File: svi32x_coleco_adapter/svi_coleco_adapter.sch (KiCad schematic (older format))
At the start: 62 parts, among them J1 Conn_01x09, J2 Conn_01x09, J3 COLECO cartridge slot, J4 SVI external bus connector, T1 NPN_BCE_9014B, T2 NPN_BCE_9014B, U1 74LS244, U10 27C64, U11 L79L05, U2 74LS244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

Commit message: Add files via upload
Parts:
- added C30, C31, C32, C33, C34, C35, C36, C37: 100nf, Capacitor_THT:C_Disc_D7.0mm_W2.5mm_P5.00mm, symbol agg-kicad:C
- C1, C12, C14, C15, C16, C19, C2, C21, C3, C4, C5, C6, C7, C8, C9: footprint Capacitor_THT:C_Disc_D7.5mm_W5.0mm_P7.50mm -> Capacitor_THT:C_Disc_D7.0mm_W2.5mm_P5.00mm
- C20: footprint Capacitor_THT:CP_Radial_D12.5mm_P5.00mm -> Capacitor_THT:CP_Radial_D8.0mm_P5.00mm
- R12, R14: value 22R -> 22K
- renumbered L2 to L1, L1 to L2
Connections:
- net +5V: now also C30.1, C31.1, C32.1, C33.1, C34.1, C35.1, C36.1, C37.1; no longer C21.1, L1.2
- net 5V: no longer J3.30 (Pin_30)
- net GND: now also C30.2, C31.2, C32.2, C33.2, C34.2, C35.2, C36.2, C37.2
- new net 5V_COL: C21.1, J3.30 (Pin_30), L1.2
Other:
- moved on the sheet: C15, C21, C24, L1, L2

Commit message: Add files via upload
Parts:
- added R40, R41: 10K, Resistor_THT:R_Axial_DIN0207_L6.3mm_D2.5mm_P10.16mm_Horizontal, symbol agg-kicad:R
- T1, T2: value NPN_BCE_9014B -> NPN_CBE_BC547B (was 9014B); symbol Device:Q_NPN_BCE -> Device:Q_NPN_CBE
- U10: value 27C64 -> 27C256; symbol Memory_EPROM:27C64 -> Memory_EPROM:27C256
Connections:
- net +5V: now also R40.1, R41.1
- net GND: now also U10.26 (A13); no longer U10.14 (GND)
- net _RAMDIS: now also U10.14 (GND)
- net at U10.1 (VPP): now also R40.2
- net at U10.27 (A14): now also R41.2
- net at C14.2, R14.2: now also T1.2 (B); no longer T1.1 (B)
- net at R3.2: now also T1.1 (C); no longer T1.2 (C)
- net at C8.2, R12.2: now also T2.2 (B); no longer T2.1 (B)
- net at R7.2: now also T2.1 (C); no longer T2.2 (C)
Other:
- note added: "(or 27C128 or 27C64)"
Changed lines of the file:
@@
 $EndComp
 $Comp
-L Memory_EPROM:27C64 U10
+L Memory_EPROM:27C256 U10
 U 1 1 63F11D97
-P 2800 3250
-F 0 "U10" H 2600 4250 50  0000 C CNN
-F 1 "27C64" H 3000 4200 50  0000 C CNN
-F 2 "Package_DIP:DIP-28_W15.24mm" H 2800 3250 50  0001 C CNN
-F 3 "http://ww1.microchip.com/downloads/en/DeviceDoc/11107M.pdf" H 2800 3250 50  0001 C CNN
-	1    2800 3250
+P 2800 3350
+F 0 "U10" H 2600 4350 50  0000 C CNN
+F 1 "27C256" H 3000 4450 50  0000 C CNN
+F 2 "Package_DIP:DIP-28_W15.24mm" H 2800 3350 50  0001 C CNN
+F 3 "http://ww1.microchip.com/downloads/en/DeviceDoc/11107M.pdf" H 2800 3350 50  0001 C CNN
+	1    2800 3350
 	1    0    0    -1
 $EndComp
@@
 Wire Wire Line
 	4150 7350 3600 7350
-Wire Wire Line
-	2400 4050 2400 4150
-Wire Wire Line
-	2400 4150 2400 4450
-Connection ~ 2400 4150
 Connection ~ 2400 4450
 Wire Wire Line
-	2400 4450 4150 4450
+	2400 4450 2800 4450
 $Comp
 L Diode:1N4001 D4
@@
 	11150 1000 11600 1000
 $Comp
-L Device:Q_NPN_BCE T1
+L Device:Q_NPN_CBE T1
 U 1 1 655A1170
 P 10200 8650
 F 0 "T1" V 10435 8650 50  0000 C CNN
-F 1 "NPN_BCE_9014B" V 10526 8650 50  0000 C CNN
+F 1 "NPN_CBE_BC547B (was 9014B)" V 10526 8650 50  0000 C CNN
 F 2 "Connector_PinHeader_2.54mm:PinHeader_1x03_P2.54mm_Vertical" H 10400 8750 50  0001 C CNN
 F 3 "~" H 10200 8650 50  0001 C CNN
@@
 $EndComp
 $Comp
-L Device:Q_NPN_BCE T2
+L Device:Q_NPN_CBE T2
 U 1 1 655B8D13
 P 11800 8650
 F 0 "T2" V 12035 8650 50  0000 C CNN
-F 1 "NPN_BCE_9014B" V 12126 8650 50  0000 C CNN
+F 1 "NPN_CBE_BC547B  (was 9014B)" V 12126 8650 50  0000 C CNN
 F 2 "Connector_PinHeader_2.54mm:PinHeader_1x03_P2.54mm_Vertical" H 12000 8750 50  0001 C CNN
 F 3 "~" H 11800 8650 50  0001 C CNN
@@
 Wire Wire Line
 	8150 600  8400 600
+$Comp
+L agg-kicad:R R40
+U 1 1 6421B2AD
+P 1900 4050
+F 0 "R40" H 1950 4231 50  0000 C CNN
+F 1 "10K" H 1950 4140 50  0000 C CNN
+F 2 "Resistor_THT:R_Axial_DIN0207_L6.3mm_D2.5mm_P10.16mm_Horizontal" H 1900 4050 50  0001 C CNN
+F 3 "" H 1900 4050 50  0001 C CNN
+	1    1900 4050
+	1    0    0    -1
+$EndComp
+$Comp
+L power:+5V #PWR0111
+U 1 1 64223787
+P 1800 3800
+F 0 "#PWR0111" H 1800 3650 50  0001 C CNN
+F 1 "+5V" H 1815 3973 50  0000 C CNN
+F 2 "" H 1800 3800 50  0001 C CNN
+F 3 "" H 1800 3800 50  0001 C CNN
+	1    1800 3800
+	1    0    0    -1
+$EndComp
+$Comp
+L power:GND #PWR0149
+U 1 1 6436A54D
+P 2050 4200
+F 0 "#PWR0149" H 2050 3950 50  0001 C CNN
+F 1 "GND" H 2055 4027 50  0000 C CNN
+F 2 "" H 2050 4200 50  0001 C CNN
+F 3 "" H 2050 4200 50  0001 C CNN
+	1    2050 4200
+	0    1    1    0
+$EndComp
+$Comp
+L agg-kicad:R R41
+U 1 1 643BE130
+P 1850 3850
+F 0 "R41" H 1900 4031 50  0000 C CNN
+F 1 "10K" H 1900 3940 50  0000 C CNN
+F 2 "Resistor_THT:R_Axial_DIN0207_L6.3mm_D2.5mm_P10.16mm_Horizontal" H 1850 3850 50  0001 C CNN
+F 3 "" H 1850 3850 50  0001 C CNN
+	1    1850 3850
+	1    0    0    -1
+$EndComp
+Wire Wire Line
+	2050 3750 2400 3750
+Wire Wire Line
+	2050 3750 2050 4200
+Text Notes 2850 2200 0    50   ~ 0
+(or 27C128 or 27C64)
+Wire Wire Line
+	2400 4250 2400 4450
+Connection ~ 2800 4450
+Wire Wire Line
+	2800 4450 4150 4450
+Wire Wire Line
+	2400 4150 2400 4250
+Connection ~ 2400 4250
+Wire Wire Line
+	2400 4050 2000 4050
+Wire Wire Line
+	1900 4050 1800 4050
+Wire Wire Line
+	1800 4050 1800 3850
+Wire Wire Line
+	2400 3850 1950 3850
+Wire Wire Line
+	1850 3850 1800 3850
+Connection ~ 1800 3850
+Wire Wire Line
+	1800 3850 1800 3800
 $EndSCHEMATC

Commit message: Add files via upload
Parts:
- J3: footprint Connector:COLECO_30_PIN -> Connector:COLECO_30_PIN_5_02
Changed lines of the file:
@@
 F 0 "J3" H 4700 3867 50  0000 C CNN
 F 1 "COLECO cartridge slot" H 4700 3776 50  0000 C CNN
-F 2 "Connector:COLECO_30_PIN" H 4650 2950 50  0001 C CNN
+F 2 "Connector:COLECO_30_PIN_5_02" H 4650 2950 50  0001 C CNN
 F 3 "" H 4650 2950 50  0001 C CNN
 	1    4650 2950

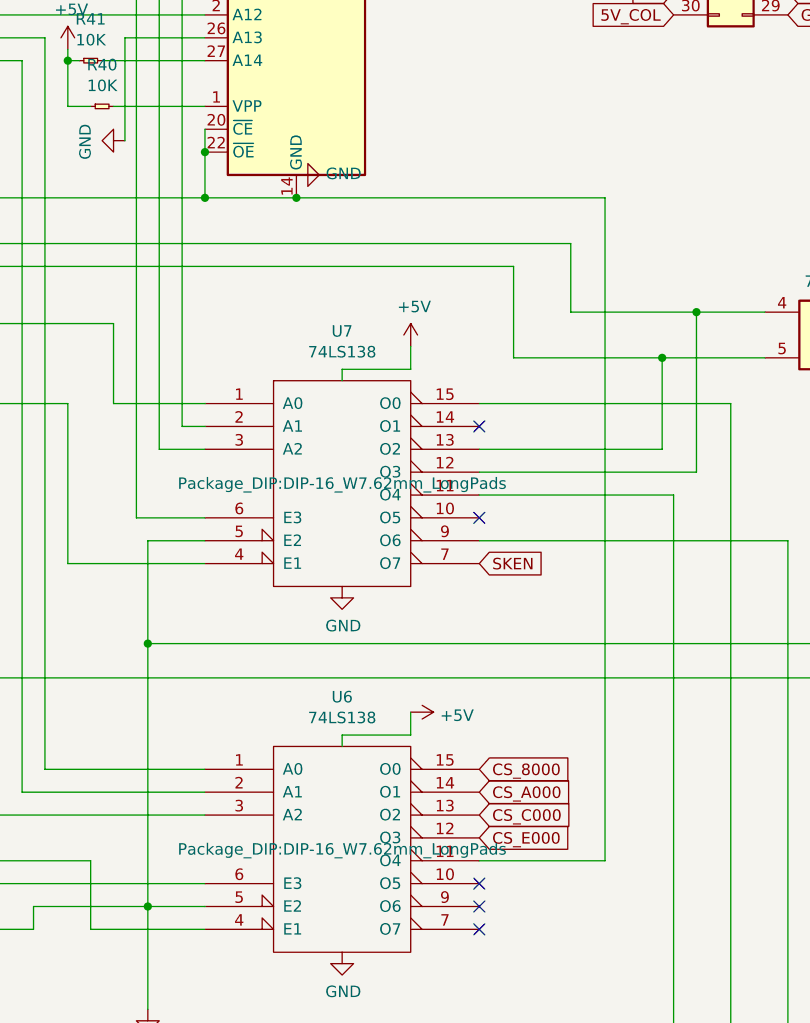
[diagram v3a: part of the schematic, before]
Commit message: Add files via upload
corrected schematics, rom group pin was invalidly connected to _RAMDIS
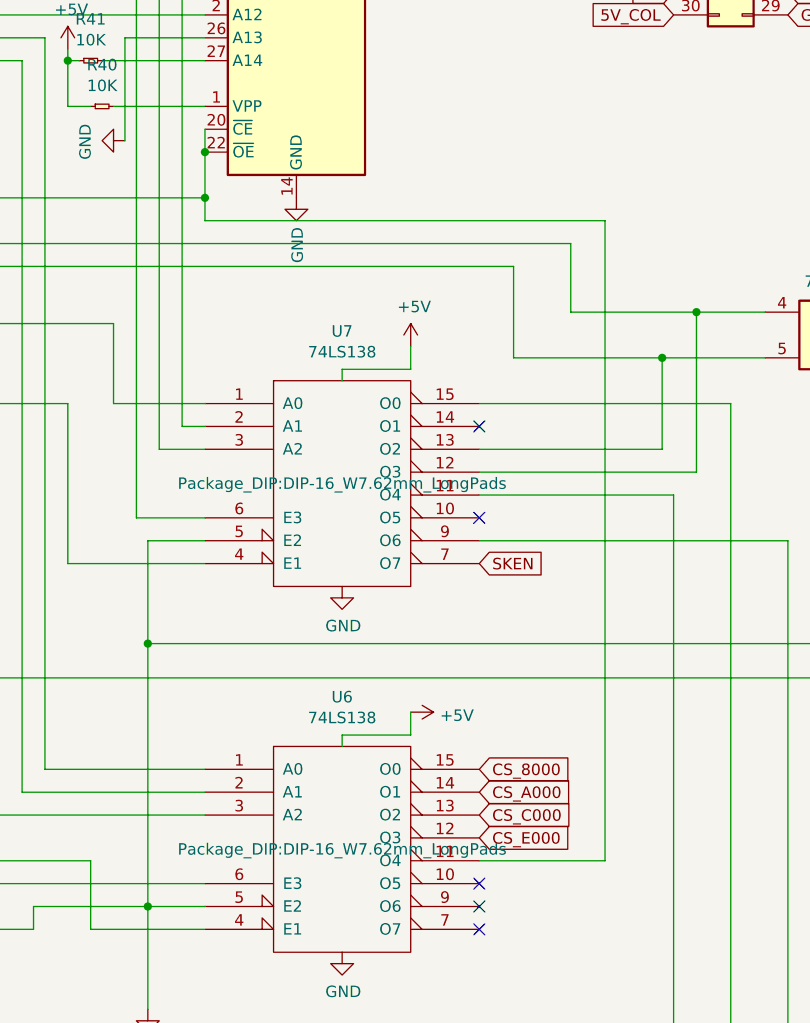
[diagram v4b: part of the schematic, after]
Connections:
- net GND: now also U10.14 (GND)
- net _RAMDIS: no longer U10.14 (GND)
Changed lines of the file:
@@
 	1000 4450 2400 4450
-Wire Wire Line
-	4150 4450 4150 7350
 Wire Wire Line
 	4150 7350 3600 7350
 Connection ~ 2400 4450
-Wire Wire Line
-	2400 4450 2800 4450
 $Comp
 L Diode:1N4001 D4
@@
 L power:GND #PWR0125
 U 1 1 64C63349
-P 2800 4350
-F 0 "#PWR0125" H 2800 4100 50  0001 C CNN
-F 1 "GND" V 2805 4222 50  0000 R CNN
-F 2 "" H 2800 4350 50  0001 C CNN
-F 3 "" H 2800 4350 50  0001 C CNN
-	1    2800 4350
-	0    -1   -1   0
+P 2800 4450
+F 0 "#PWR0125" H 2800 4200 50  0001 C CNN
+F 1 "GND" V 2805 4322 50  0000 R CNN
+F 2 "" H 2800 4450 50  0001 C CNN
+F 3 "" H 2800 4450 50  0001 C CNN
+	1    2800 4450
+	1    0    0    -1
 $EndComp
 Wire Wire Line
@@
 Wire Wire Line
 	2400 4250 2400 4450
-Connection ~ 2800 4450
-Wire Wire Line
-	2800 4450 4150 4450
 Wire Wire Line
 	2400 4150 2400 4250
@@
 Wire Wire Line
 	1800 3850 1800 3800
+Wire Wire Line
+	2400 4450 2400 4550
+Wire Wire Line
+	2400 4550 4150 4550
+Wire Wire Line
+	4150 4550 4150 7350
 $EndSCHEMATC

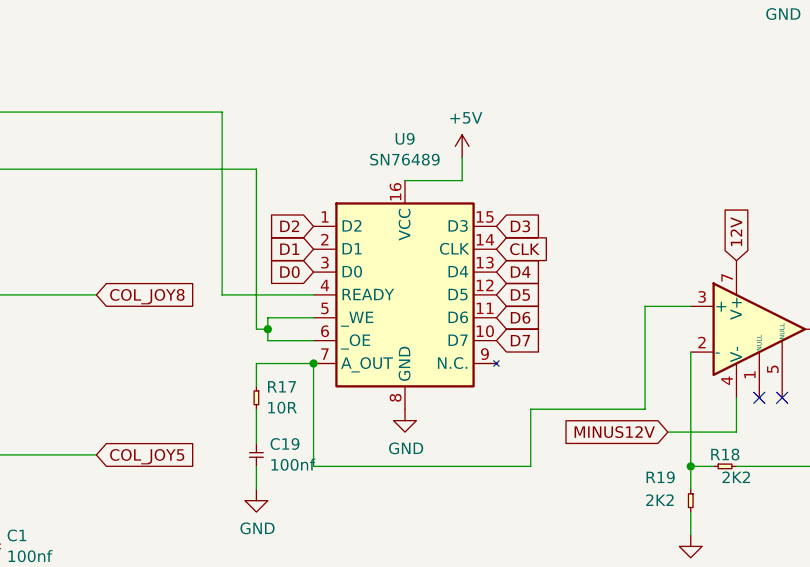
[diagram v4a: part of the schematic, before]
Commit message: Add files via upload
corrected audio chip SN76489  data pin connections to datalines to reversed order, so that D0 is connected to SN76489 pin D7, D1 to pin D6, pin D2 to pin D5 and so on.
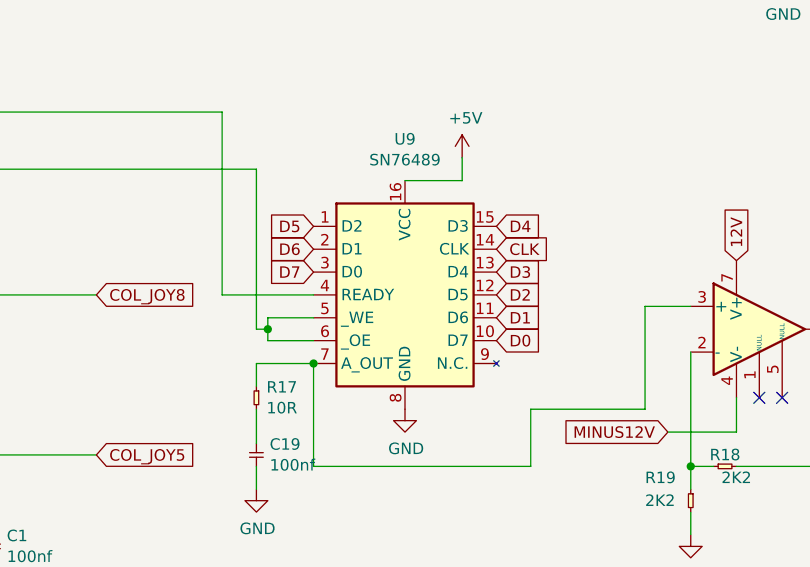
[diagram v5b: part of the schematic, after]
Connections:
- net D0: now also U9.10 (D7); no longer U9.3 (D0)
- net D1: now also U9.11 (D6); no longer U9.2 (D1)
- net D2: now also U9.12 (D5); no longer U9.1 (D2)
- net D3: now also U9.13 (D4); no longer U9.15 (D3)
- net D4: now also U9.15 (D3); no longer U9.13 (D4)
- net D5: now also U9.1 (D2); no longer U9.12 (D5)
- net D6: now also U9.2 (D1); no longer U9.11 (D6)
- net D7: now also U9.3 (D0); no longer U9.10 (D7)
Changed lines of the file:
@@
 	1    0    0    -1
 $EndComp
+Text GLabel 9450 10550 2    50   Input ~ 0
+D0
+Text GLabel 9450 10350 2    50   Input ~ 0
+D2
+Text GLabel 9450 10450 2    50   Input ~ 0
+D1
 Text GLabel 8650 10250 0    50   Input ~ 0
-D0
+D7
+Text GLabel 8650 10150 0    50   Input ~ 0
+D6
 Text GLabel 8650 10050 0    50   Input ~ 0
-D2
-Text GLabel 8650 10150 0    50   Input ~ 0
-D1
-Text GLabel 9450 10550 2    50   Input ~ 0
-D7
-Text GLabel 9450 10450 2    50   Input ~ 0
-D6
-Text GLabel 9450 10350 2    50   Input ~ 0
 D5
+Text GLabel 9450 10050 2    50   Input ~ 0
+D4
 Text GLabel 9450 10250 2    50   Input ~ 0
-D4
-Text GLabel 9450 10050 2    50   Input ~ 0
 D3
 Text GLabel 9450 10150 2    50   Input ~ 0
